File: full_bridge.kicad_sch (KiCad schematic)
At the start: 0 parts

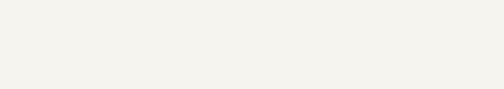
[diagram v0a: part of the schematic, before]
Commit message: schematic: continue project architecture
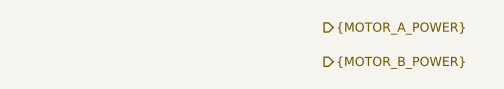
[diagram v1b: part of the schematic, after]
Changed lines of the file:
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@@
+		)
+	)
+	(hierarchical_label "{MOTOR_A_POWER}"
+		(shape output)
+		(at 194.31 59.69 0)
+		(effects
+			(font
+				(size 1.016 1.016)
+			)
+			(justify left)
+		)
+	)
+	(hierarchical_label "{MOTOR_B_POWER}"
+		(shape output)
+		(at 194.31 63.5 0)
+		(effects
+			(font
+				(size 1.016 1.016)
+			)
+			(justify left)
 		)
 	)

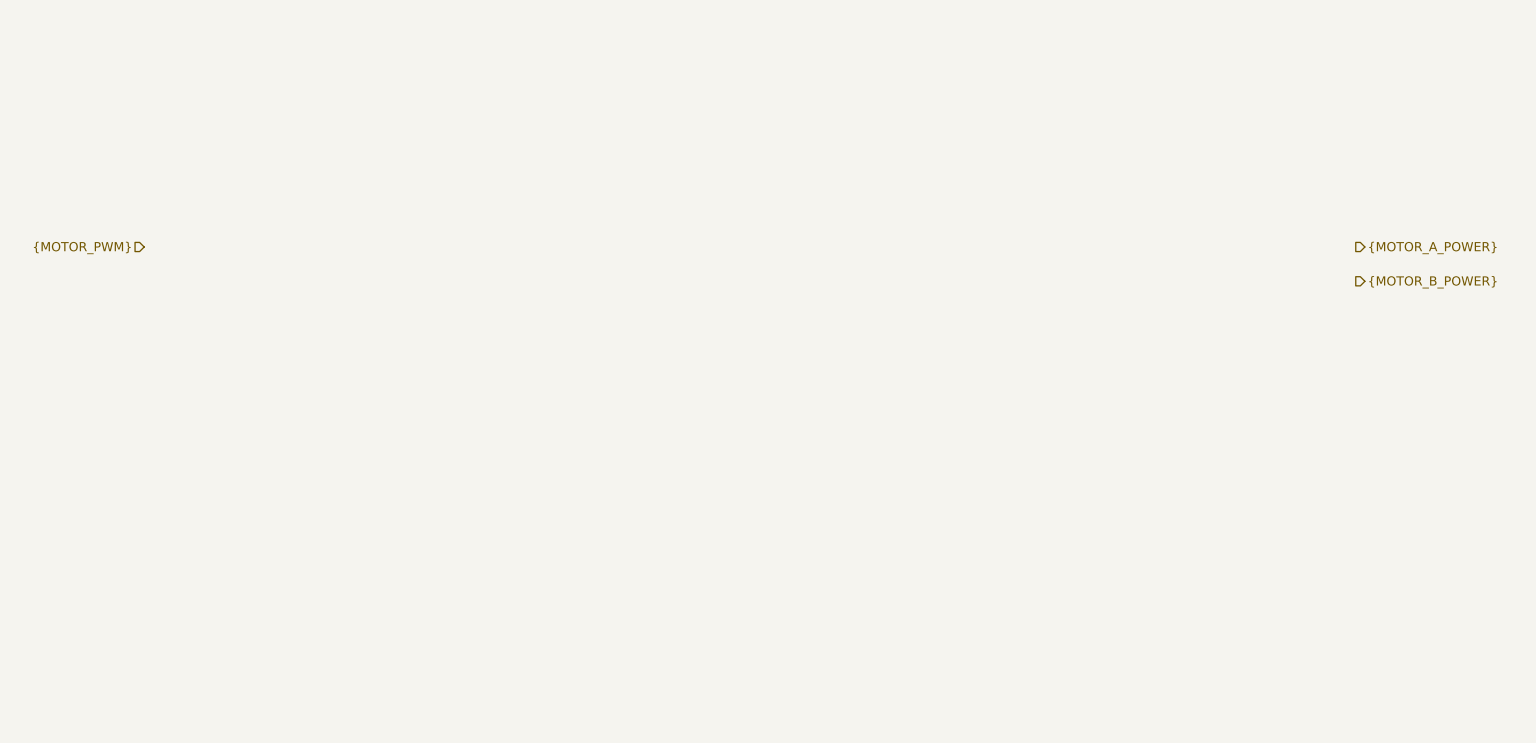
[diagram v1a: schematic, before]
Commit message: schematic: add project structure wiring
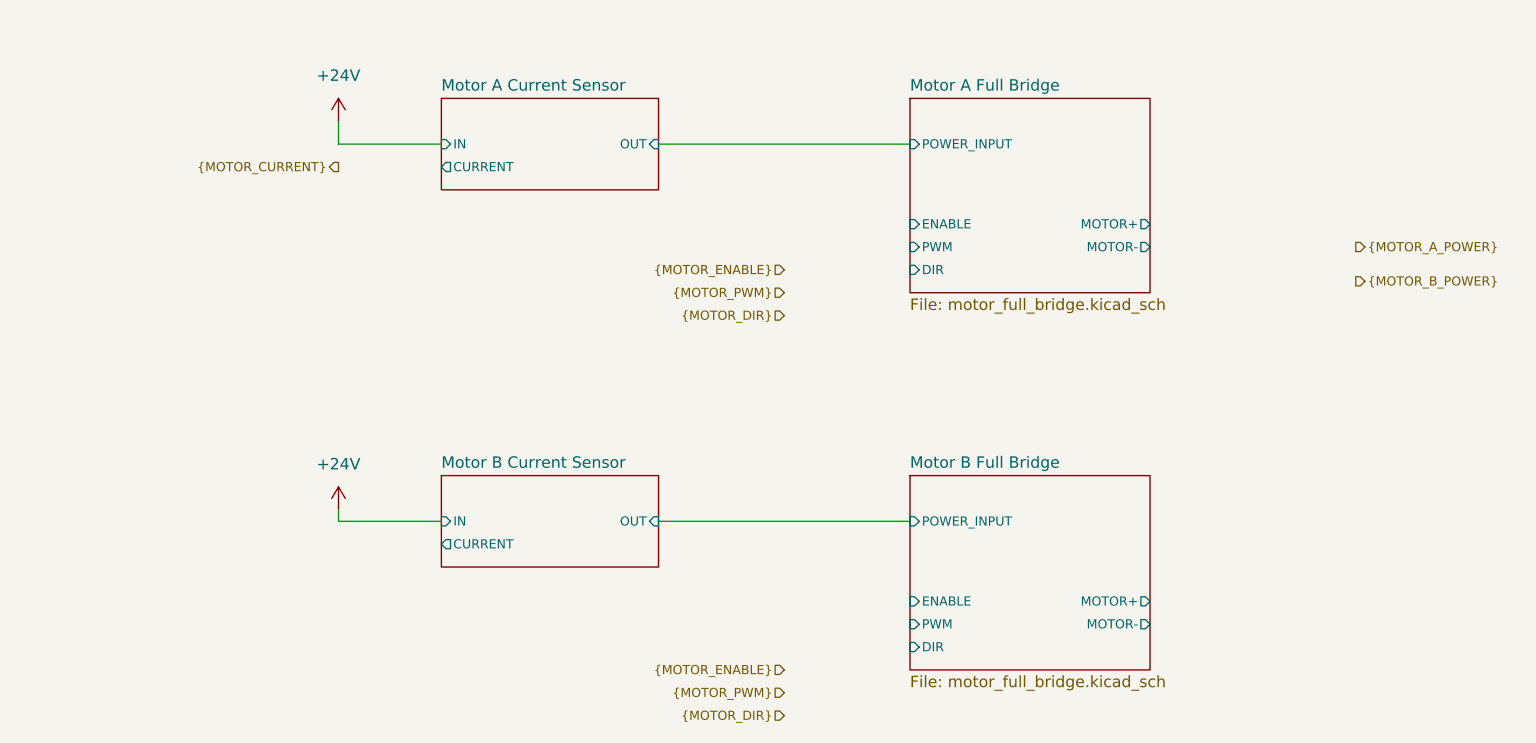
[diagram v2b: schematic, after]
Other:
- added sheet Motor A Current Sensor (motor_current_sensor.kicad_sch)
- added sheet Motor A Full Bridge (motor_full_bridge.kicad_sch)
- added sheet Motor B Current Sensor (motor_current_sensor.kicad_sch)
- added sheet Motor B Full Bridge (motor_full_bridge.kicad_sch)

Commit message: Add power stages
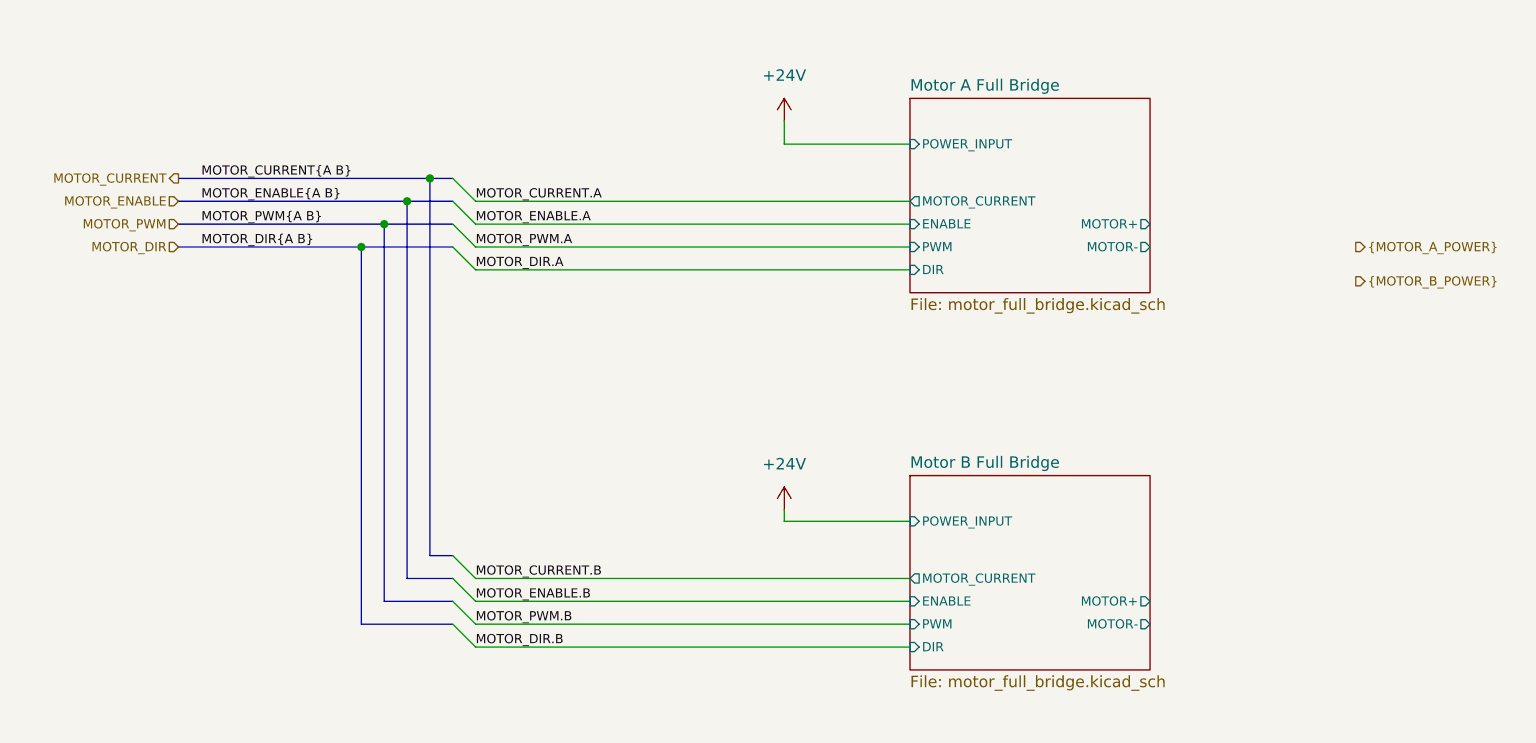
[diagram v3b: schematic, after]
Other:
- removed sheet Motor A Current Sensor
- removed sheet Motor B Current Sensor
- sheet Motor A Full Bridge ports: added MOTOR_CURRENT; removed none
- sheet Motor B Full Bridge ports: added MOTOR_CURRENT; removed none

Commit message: Add power supplies
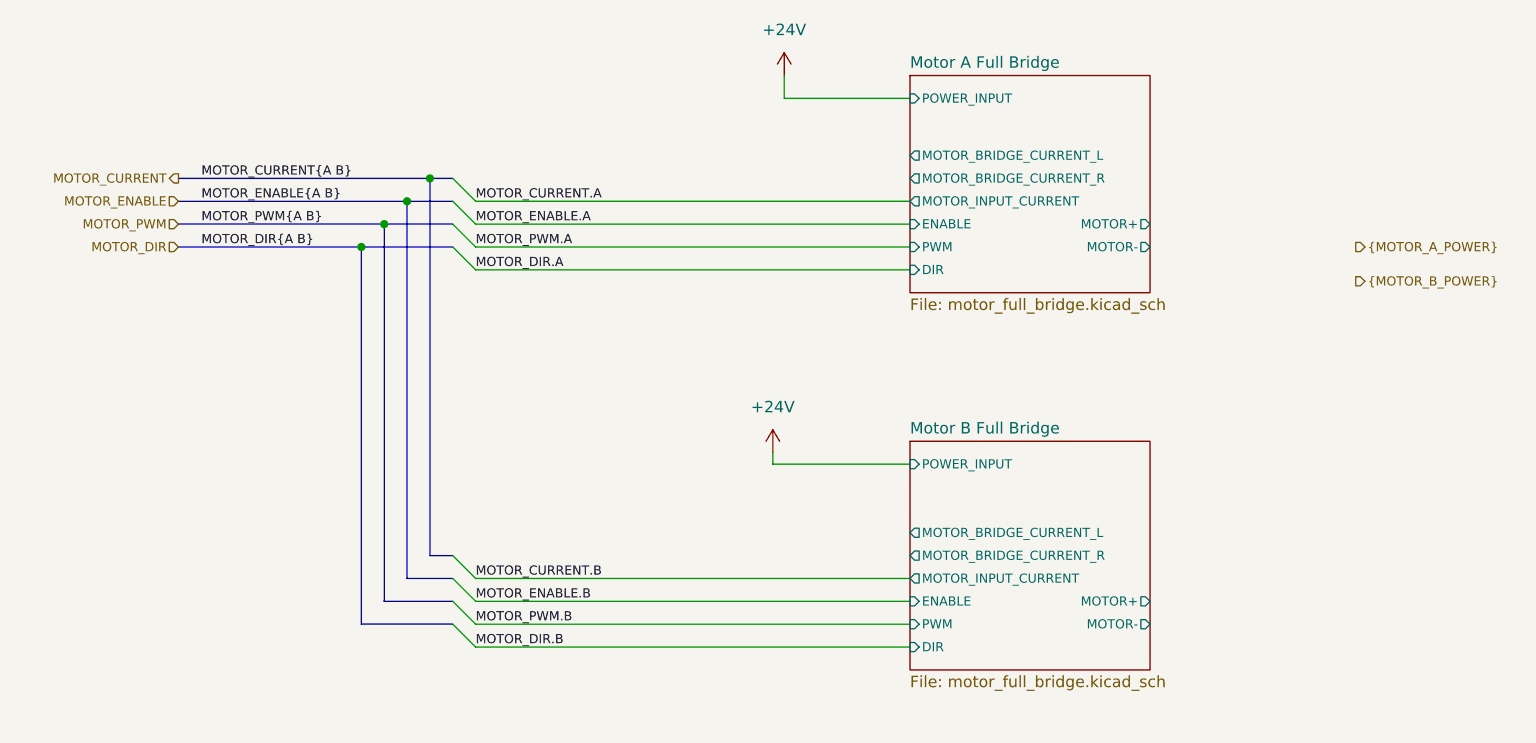
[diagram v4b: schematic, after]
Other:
- sheet Motor A Full Bridge ports: added MOTOR_BRIDGE_CURRENT_L, MOTOR_BRIDGE_CURRENT_R, MOTOR_INPUT_CURRENT; removed MOTOR_CURRENT
- sheet Motor B Full Bridge ports: added MOTOR_BRIDGE_CURRENT_L, MOTOR_BRIDGE_CURRENT_R, MOTOR_INPUT_CURRENT; removed MOTOR_CURRENT
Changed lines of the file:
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@@
 	(wire
 		(pts
-			(xy 130.81 90.17) (xy 144.78 90.17)
+			(xy 129.54 83.82) (xy 144.78 83.82)
 		)
 		(stroke
@@
 	(wire
 		(pts
-			(xy 130.81 45.72) (xy 130.81 48.26)
+			(xy 130.81 40.64) (xy 130.81 43.18)
 		)
 		(stroke
@@
 	(wire
 		(pts
-			(xy 130.81 48.26) (xy 144.78 48.26)
+			(xy 130.81 43.18) (xy 144.78 43.18)
 		)
 		(stroke
@@
 	(wire
 		(pts
-			(xy 130.81 88.9) (xy 130.81 90.17)
+			(xy 129.54 82.55) (xy 129.54 83.82)
 		)
 		(stroke
@@
 	(symbol
 		(lib_id "power:+24V")
-		(at 130.81 88.9 0)
+		(at 129.54 82.55 0)
 		(unit 1)
 		(exclude_from_sim no)
@@
 		(fields_autoplaced yes)
 		(property "Reference" "#PWR01602"
-			(at 130.81 92.71 0)
+			(at 129.54 86.36 0)
 			(effects
 				(font
@@
 		)
 		(property "Value" "+24V"
-			(at 130.81 83.82 0)
+			(at 129.54 77.47 0)
 			(effects
 				(font
@@
 		)
 		(property "Footprint" ""
-			(at 130.81 88.9 0)
+			(at 129.54 82.55 0)
 			(effects
 				(font
@@
 		)
 		(property "Datasheet" ""
-			(at 130.81 88.9 0)
+			(at 129.54 82.55 0)
 			(effects
 				(font
@@
 		)
 		(property "Description" "Power symbol creates a global label with name \"+24V\""
-			(at 130.81 88.9 0)
+			(at 129.54 82.55 0)
 			(effects
 				(font
@@
 	(symbol
 		(lib_id "power:+24V")
-		(at 130.81 45.72 0)
+		(at 130.81 40.64 0)
 		(unit 1)
 		(exclude_from_sim no)
@@
 		(fields_autoplaced yes)
 		(property "Reference" "#PWR01601"
-			(at 130.81 49.53 0)
+			(at 130.81 44.45 0)
 			(effects
 				(font
@@
 		)
 		(property "Value" "+24V"
+			(at 130.81 35.56 0)
+			(effects
+				(font
+					(size 1.27 1.27)
+				)
+			)
+		)
+		(property "Footprint" ""
 			(at 130.81 40.64 0)
 			(effects
@@
 					(size 1.27 1.27)
 				)
-			)
-		)
-		(property "Footprint" ""
-			(at 130.81 45.72 0)
-			(effects
-				(font
-					(size 1.27 1.27)
-				)
 				(hide yes)
 			)
 		)
 		(property "Datasheet" ""
-			(at 130.81 45.72 0)
+			(at 130.81 40.64 0)
 			(effects
 				(font
@@
 		)
 		(property "Description" "Power symbol creates a global label with name \"+24V\""
-			(at 130.81 45.72 0)
+			(at 130.81 40.64 0)
 			(effects
 				(font
@@
 	)
 	(sheet
-		(at 144.78 43.18)
-		(size 26.67 21.59)
+		(at 144.78 40.64)
+		(size 26.67 24.13)
 		(exclude_from_sim no)
 		(in_bom yes)
@@
 		)
 		(property "Sheetname" "Motor A Full Bridge"
-			(at 144.78 42.4684 0)
+			(at 144.78 39.9284 0)
 			(effects
 				(font
@@
 		)
 		(pin "POWER_INPUT" input
-			(at 144.78 48.26 180)
+			(at 144.78 43.18 180)
 			(effects
 				(font
@@
 			)
 		)
-		(pin "MOTOR_CURRENT" output
+		(pin "MOTOR_BRIDGE_CURRENT_L" output
+			(at 144.78 49.53 180)
+			(effects
+				(font
+					(size 1.016 1.016)
+				)
+				(justify left)
+			)
+		)
+		(pin "MOTOR_BRIDGE_CURRENT_R" output
+			(at 144.78 52.07 180)
+			(effects
+				(font
+					(size 1.016 1.016)
+				)
+				(justify left)
+			)
+		)
+		(pin "MOTOR_INPUT_CURRENT" output
 			(at 144.78 54.61 180)
 			(effects
@@
 	)
 	(sheet
-		(at 144.78 85.09)
-		(size 26.67 21.59)
+		(at 144.78 81.28)
+		(size 26.67 25.4)
 		(exclude_from_sim no)
 		(in_bom yes)
@@
 		)
 		(property "Sheetname" "Motor B Full Bridge"
-			(at 144.78 84.3784 0)
+			(at 144.78 80.5684 0)
 			(effects
 				(font
@@
 		)
 		(pin "POWER_INPUT" input
-			(at 144.78 90.17 180)
+			(at 144.78 83.82 180)
 			(effects
 				(font
@@
 			)
 		)
-		(pin "MOTOR_CURRENT" output
+		(pin "MOTOR_BRIDGE_CURRENT_L" output
+			(at 144.78 91.44 180)
+			(effects
+				(font
+					(size 1.016 1.016)
+				)
+				(justify left)
+			)
+		)
+		(pin "MOTOR_BRIDGE_CURRENT_R" output
+			(at 144.78 93.98 180)
+			(effects
+				(font
+					(size 1.016 1.016)
+				)
+				(justify left)
+			)
+		)
+		(pin "MOTOR_INPUT_CURRENT" output
 			(at 144.78 96.52 180)
 			(effects
